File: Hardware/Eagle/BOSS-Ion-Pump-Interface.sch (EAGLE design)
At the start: 27 parts, among them J4 PINHD-1X2-MOLEX-22112022, U1 ISO224ADWVR, U2 ISO224ADWVR

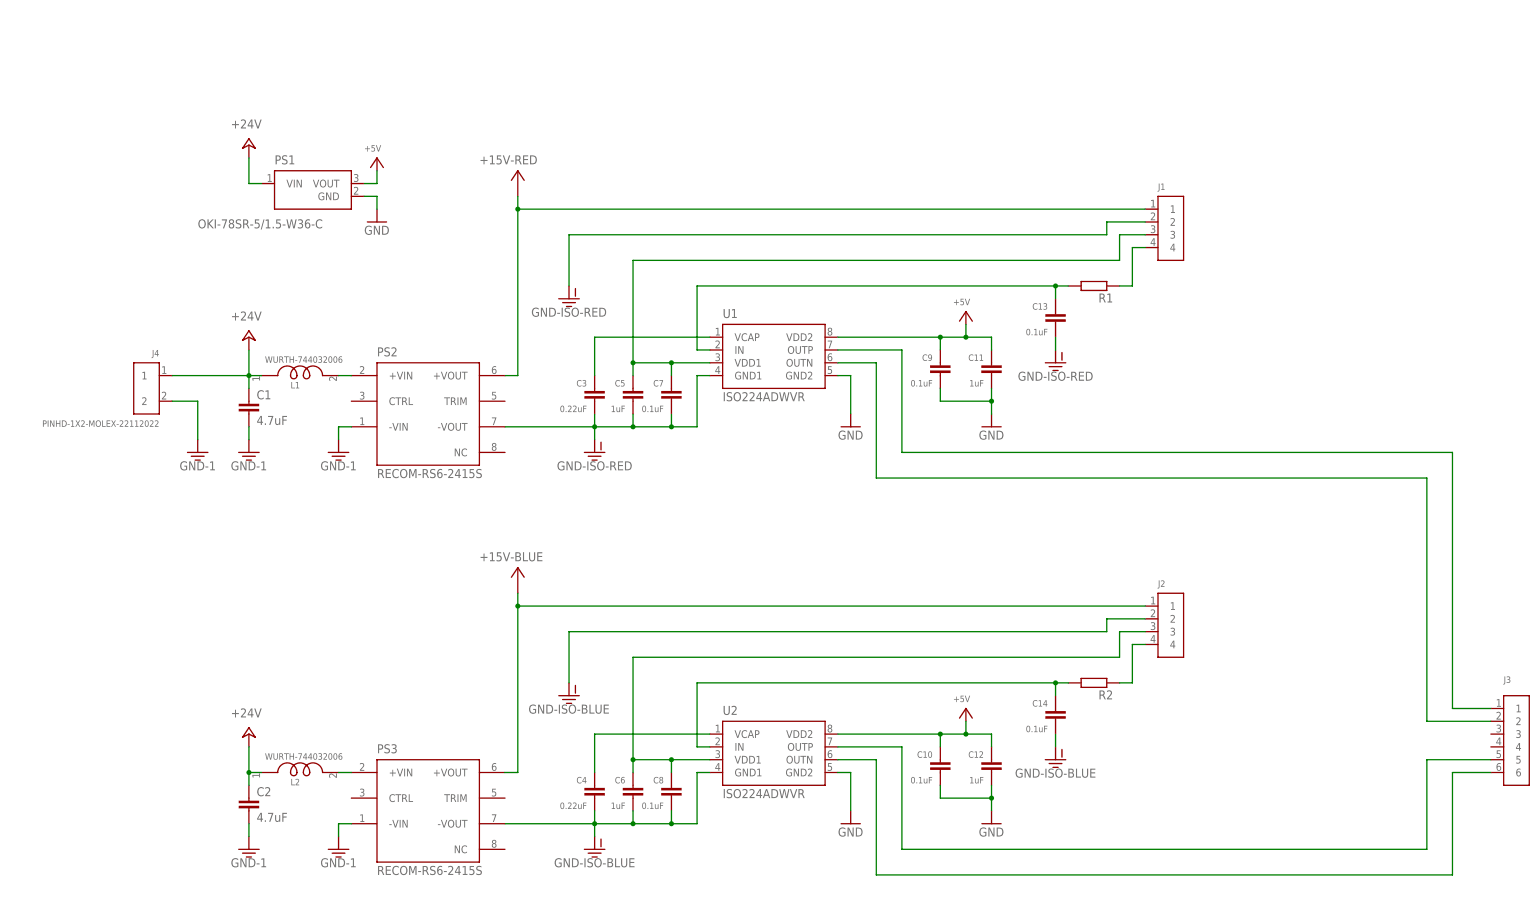
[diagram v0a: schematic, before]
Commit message: Increased capacitor voltages and changed to 1206
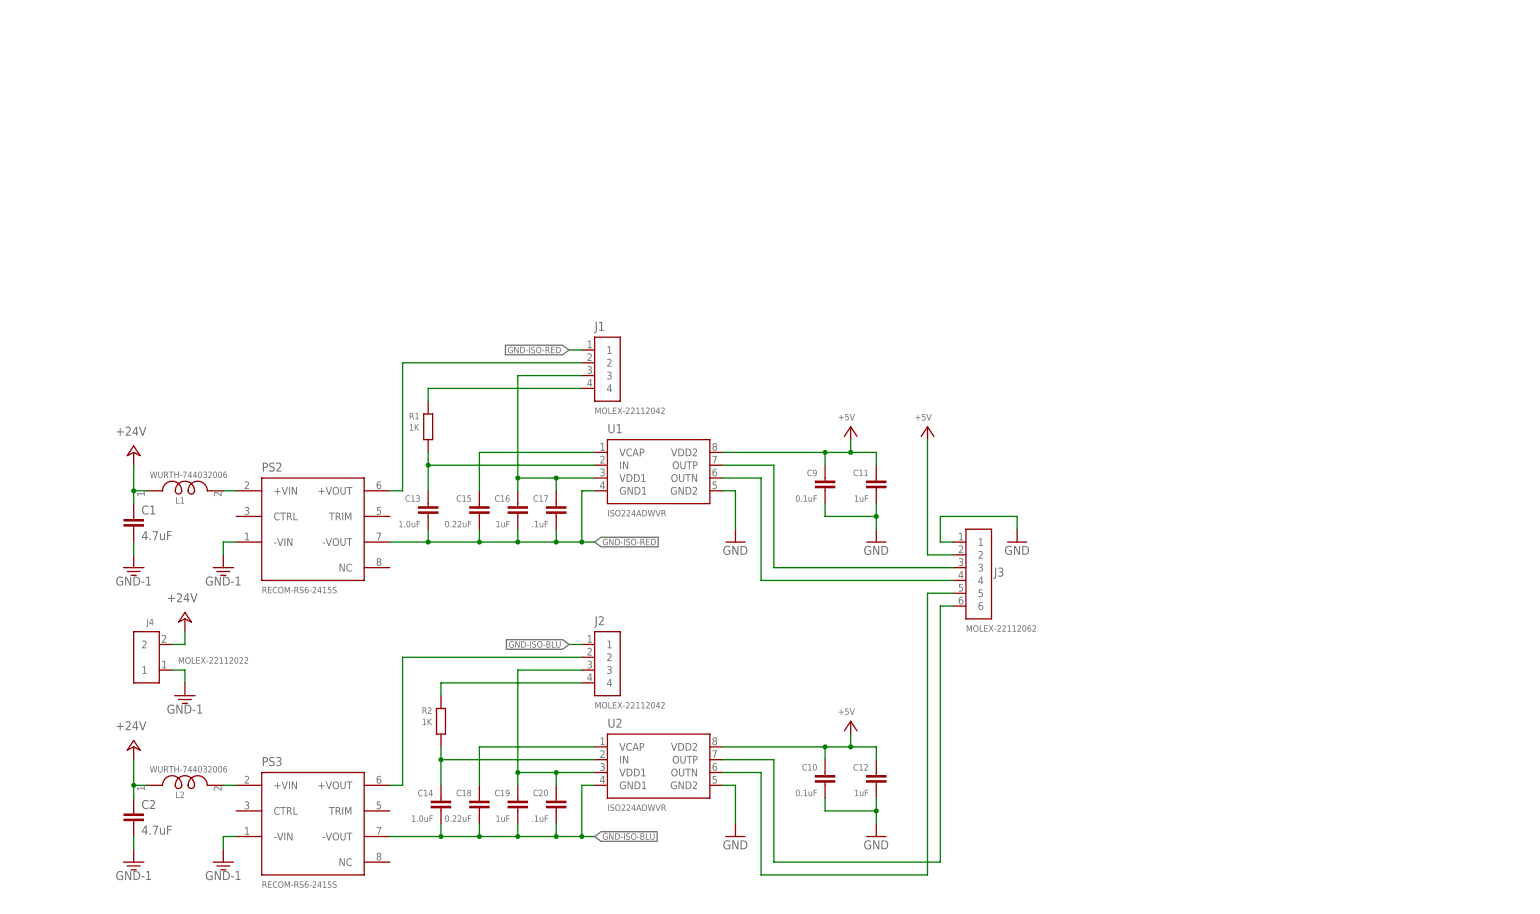
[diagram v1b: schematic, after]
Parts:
- removed C3, C4: 0.22uF, AUmlib:C-EUC0805
- removed C5, C6: 1uF, AUmlib:C-EUC0805
- removed C7, C8: 0.1uF, AUmlib:C-EUC0805
- removed PS1: OKI-78SR-5/1.5-W36-C, AUmlib:OKI-78SR-5/1.5-W36-C
- added C15, C18: 0.22uF, AUmlib:C-EUC1206
- added C16, C19: 1uF, AUmlib:C-EUC1206
- added C17, C20: .1uF, AUmlib:C-EUC1206
- C13, C14: value 0.1uF -> 1.0uF
- J1, J2: value (none) -> MOLEX-22112042
- J3: value (none) -> MOLEX-22112062
- J4: value PINHD-1X2-MOLEX-22112022 -> MOLEX-22112022
- R1, R2: value (none) -> 1K
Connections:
- net N$1 renamed IN-RED
- net N$12 renamed IN-BLUE
- removed net GND-ISO-1: C13.2, C3.2, C5.2, C7.2, J1.2, PS2.-VOUT, U1.GND1
- removed net GND-ISO-2: C14.2, C4.2, C6.2, C8.2, J2.2, PS3.-VOUT, U2.GND1
- removed net N$13: C6.1, C8.1, J2.3, U2.VDD1
- removed net N$3: C5.1, C7.1, J1.3, U1.VDD1
- new net GND-ISO-BLU: C14.2, C18.2, C19.2, C20.2, J2.1, PS3.-VOUT, U2.GND1
- new net GND-ISO-RED: C13.2, C15.2, C16.2, C17.2, J1.1, PS2.-VOUT, U1.GND1
- new net VDD1-BLUE: C19.1, C20.1, J2.3, U2.VDD1
- new net VDD1-RED: C16.1, C17.1, J1.3, U1.VDD1
- net +15V-BLUE: now also J2.2; no longer J2.1
- net +15V-RED: now also J1.2; no longer J1.1
- net +24V: now also J4.2; no longer J4.1, PS1.VIN
- net +5V: now also J3.2; no longer PS1.VOUT
- net BLUE+: now also J3.6; no longer J3.5
- net BLUE-: now also J3.5; no longer J3.6
- net GND: now also J3.1; no longer PS1.GND
- net GND-1: now also J4.1; no longer J4.2
- net N$2: now also C15.1; no longer C3.1
- net N$6: now also C18.1; no longer C4.1
- net RED+: now also J3.3; no longer J3.1
- net RED-: now also J3.4; no longer J3.2
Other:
- note added: "Pin 2 routes through shorting connector and toggle switch before coming back to pin 3."
- note removed: "Pin 1 routes through shorting connector and toggle switch befire coming back to pin 3."
- moved on the sheet: C1, C10, C11, C12, C13, C14, C2, C9, J1, J2, J3, J4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

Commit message: Added test points, cleaned up ERC check
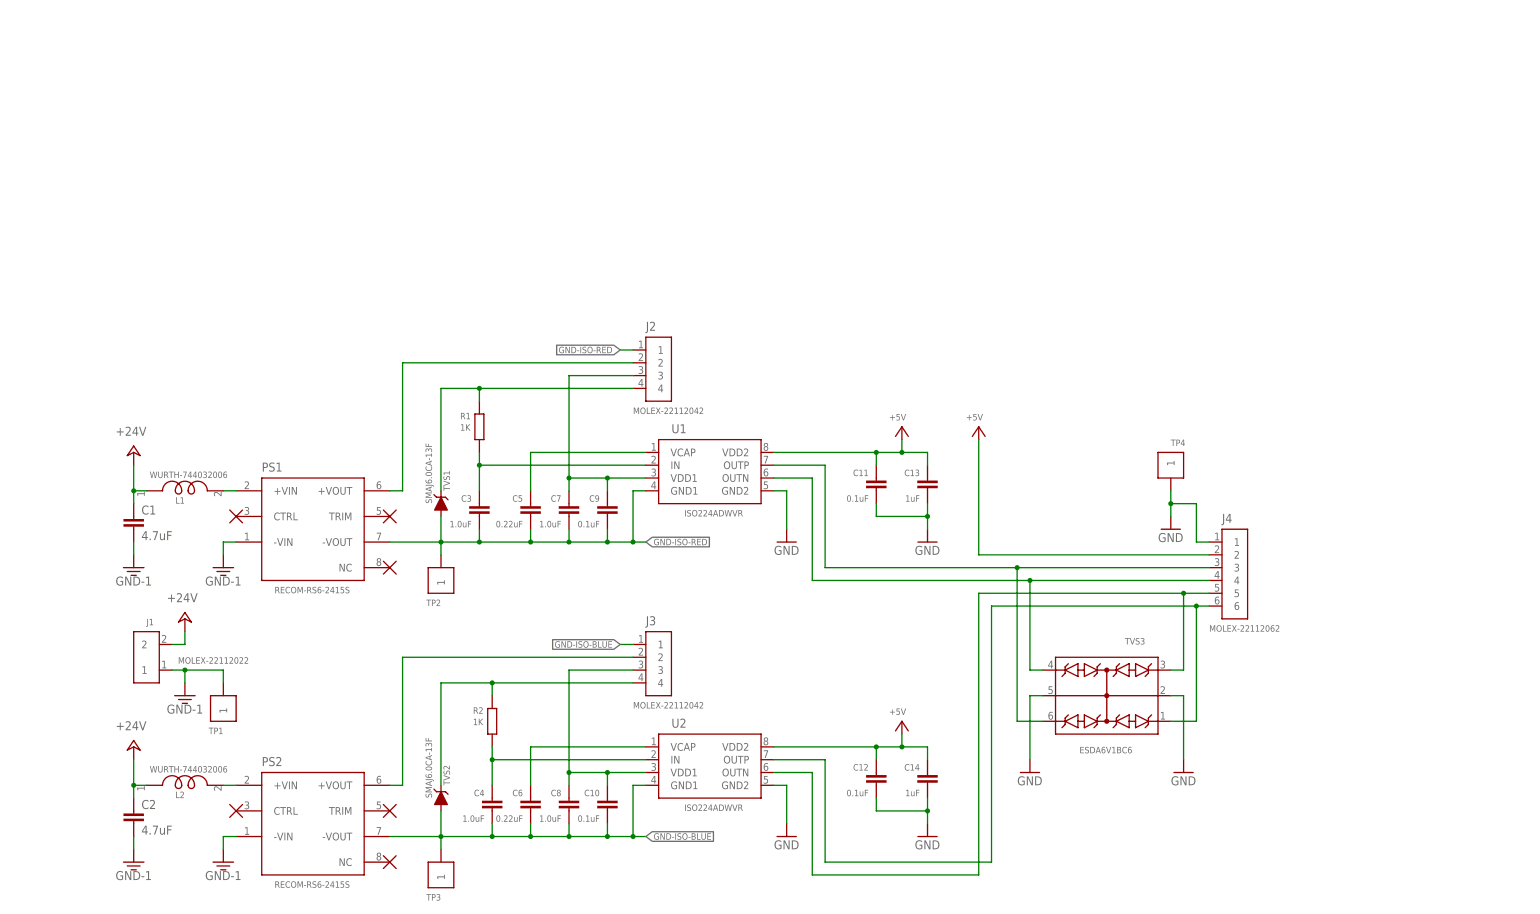
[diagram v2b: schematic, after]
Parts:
- removed C15, C18: 0.22uF, AUmlib:C-EUC1206
- removed C16, C19: 1uF, AUmlib:C-EUC1206
- removed C17, C20: .1uF, AUmlib:C-EUC1206
- removed PS3: RECOM-RS6-2415S, AUmlib:DC-DC-15V-RECOM-RS6-2415S
- added C3, C4: 1.0uF, AUmlib:C-EUC0805
- added C5, C6: 0.22uF, AUmlib:C-EUC1206
- added C7, C8: 1.0uF, AUmlib:C-EUC1206
- added PS1: RECOM-RS6-2415S, AUmlib:DC-DC-15V-RECOM-RS6-2415S
- added TP1, TP2, TP3, TP4: TP5000-TESTPOINT-BLK, AUmlib:TP5000-TESTPOINT-BLK
- added TVS1, TVS2: SMAJ6.0CA-13F, AUmlib:TVS-DIODE-SMAJ6.0CA-13-FSMA_DIO-M
- added TVS3: ESDA6V1BC6, AUmlib:TVS-QUAD-ESDA6V1BC6
- C10, C9: device AUmlib:C-EUC0805 -> AUmlib:C-EUC1206
- C11, C12: value 1uF -> 0.1uF
- C13, C14: value 1.0uF -> 1uF
- J1: value MOLEX-22112042 -> MOLEX-22112022; device AUmlib:PINHD-1X4-MOLEX-22112042 -> AUmlib:PINHD-1X2-MOLEX-22112022
- J3: value MOLEX-22112062 -> MOLEX-22112042; device AUmlib:PINHD-1X6-MOLEX-22112062 -> AUmlib:PINHD-1X4-MOLEX-22112042
- J4: value MOLEX-22112022 -> MOLEX-22112062; device AUmlib:PINHD-1X2-MOLEX-22112022 -> AUmlib:PINHD-1X6-MOLEX-22112062
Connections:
- removed net BLUE+: J3.6, U2.OUTP
- removed net BLUE-: J3.5, U2.OUTN
- removed net GND-ISO-BLU: C14.2, C18.2, C19.2, C20.2, J2.1, PS3.-VOUT, U2.GND1
- removed net N$14: J2.4, R2.1
- removed net N$2: C15.1, U1.VCAP
- removed net N$4: L1.2, PS2.+VIN
- removed net N$5: J1.4, R1.1
- removed net N$6: C18.1, U2.VCAP
- removed net N$9: L2.2, PS3.+VIN
- removed net RED+: J3.3, U1.OUTP
- removed net RED-: J3.4, U1.OUTN
- new net +VIN-BLUE: L2.2, PS2.+VIN
- new net +VIN-RED: L1.2, PS1.+VIN
- new net FROM-BLUE-PUMP: J3.4, R2.1, TVS2.C
- new net FROM-RED-PUMP: J2.4, R1.1, TVS1.C
- new net GND-ISO-BLUE: C10.2, C4.2, C6.2, C8.2, J3.1, PS2.-VOUT, TP3.1, TVS2.A, U2.GND1
- new net OUTN-BLUE: J4.5, TVS3.C2, U2.OUTN
- new net OUTN-RED: J4.4, TVS3.C3, U1.OUTN
- new net OUTP-BLUE: J4.6, TVS3.C1, U2.OUTP
- new net OUTP-RED: J4.3, TVS3.C4, U1.OUTP
- new net VCAP-BLUE: C6.1, U2.VCAP
- new net VCAP-RED: C5.1, U1.VCAP
- net +15V-BLUE: now also J3.2, PS2.+VOUT; no longer J2.2, PS3.+VOUT
- net +15V-RED: now also J2.2, PS1.+VOUT; no longer J1.2, PS2.+VOUT
- net +24V: now also J1.2; no longer J4.2
- net +5V: now also C13.1, C14.1, J4.2; no longer C10.1, C9.1, J3.2
- net GND: now also C13.2, C14.2, J4.1, TP4.1, TVS3.CC1, TVS3.CC2; no longer C10.2, C9.2, J3.1
- net GND-1: now also J1.1, PS1.-VIN, TP1.1; no longer J4.1, PS3.-VIN
- net GND-ISO-RED: now also C3.2, C5.2, C7.2, C9.2, J2.1, PS1.-VOUT, TP2.1, TVS1.A; no longer C13.2, C15.2, C16.2, C17.2, J1.1, PS2.-VOUT
- net IN-BLUE: now also C4.1; no longer C14.1
- net IN-RED: now also C3.1; no longer C13.1
- net VDD1-BLUE: now also C10.1, C8.1, J3.3; no longer C19.1, C20.1, J2.3
- net VDD1-RED: now also C7.1, C9.1, J2.3; no longer C16.1, C17.1, J1.3
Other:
- moved on the sheet: C10, C13, C14, C9, J2, PS2, R1, R2, U1, U2

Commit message: Added external parts (switches and panel connectors)
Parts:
- added SW1, SW2: SPST-OFFBOARD, AUmlib:SPST-OFFBOARD
- added U$11, U$8, U$9: CON-CIRCULAR-6-OFF-BOARD, AUmlib:CON-CIRCULAR-6-OFF-BOARD
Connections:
- new net CASE-GND: U$8.1, U$9.1
- net +15V-BLUE: now also SW2.1
- net +15V-RED: now also SW1.1
- net +5V: now also U$11.2
- net FROM-BLUE-PUMP: now also U$9.2
- net FROM-RED-PUMP: now also U$8.2
- net GND: now also U$11.1
- net GND-ISO-BLUE: now also U$9.4
- net GND-ISO-RED: now also U$8.4
- net OUTN-BLUE: now also U$11.5
- net OUTN-RED: now also U$11.4
- net OUTP-BLUE: now also U$11.6
- net OUTP-RED: now also U$11.3
- net VDD1-BLUE: now also SW2.2, U$9.5, U$9.6
- net VDD1-RED: now also SW1.2, U$8.5, U$8.6
